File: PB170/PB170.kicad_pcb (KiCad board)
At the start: 4 copper layers, 96.5 x 71.1 mm, 34 parts, among them J1 USB_C_Receptacle_USB2.0-Conne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, J2 USB_B_Micro, Q1 P-MOSFET-MLP_HS, Q2 BC817, SW1 SW_MEC_5E, SW2 SW_MEC_5E, U1 74HC00

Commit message: KiCad crashing fixup, probably
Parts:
- removed J1: USB_C_Receptacle_USB2.0-Connector, PB170:USB_C_Female-16Pin-HPJF
- added RV1: R_POT, PB170:potentiometer10k, F.Cu at (61.6, 90.9)
- added SW3: SW_SPDT, PB170:toggleSwitch, F.Cu at (101.5, 32.3)
- added U2: 74HC08, Housings_SOIC:SOIC-14_3.9x8.7mm_Pitch1.27mm, F.Cu at (127.0, 48.5)
- added U3: 74HC4511D, Housings_SOIC:SOIC-16_3.9x9.9mm_Pitch1.27mm, F.Cu at (127.1, 63.1)
- added U4: HEF4518BT, Housings_SOIC:SOIC-16_3.9x9.9mm_Pitch1.27mm, F.Cu at (116.8, 35.7)
- added U5: 74HC32, Housings_SOIC:SOIC-14_3.9x8.7mm_Pitch1.27mm, F.Cu at (60.6, 35.4)
- J2: footprint Connectors:USB_Micro-B -> PB170:MICRO-USB-SMD_MICROXNJ; moved to F.Cu
- R10: value 220R -> 10k; footprint Resistors_SMD:R_0603 -> Resistor_SMD:R_0603_1608Metric
- moved J2 46.2 mm to (79.1, 92.2)
- moved R11 34.2 mm to (78.7, 83.8)
- moved R10 23.1 mm to (88.6, 36.4)
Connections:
- R10 pad 2: Net-(J1-PadA7) -> GND
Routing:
- net Net-(J2-Pad3): track 3.47 -> 0.00 mm, vias 1 -> 0
- net Net-(J2-Pad2): track 3.11 -> 0.00 mm, vias 1 -> 0

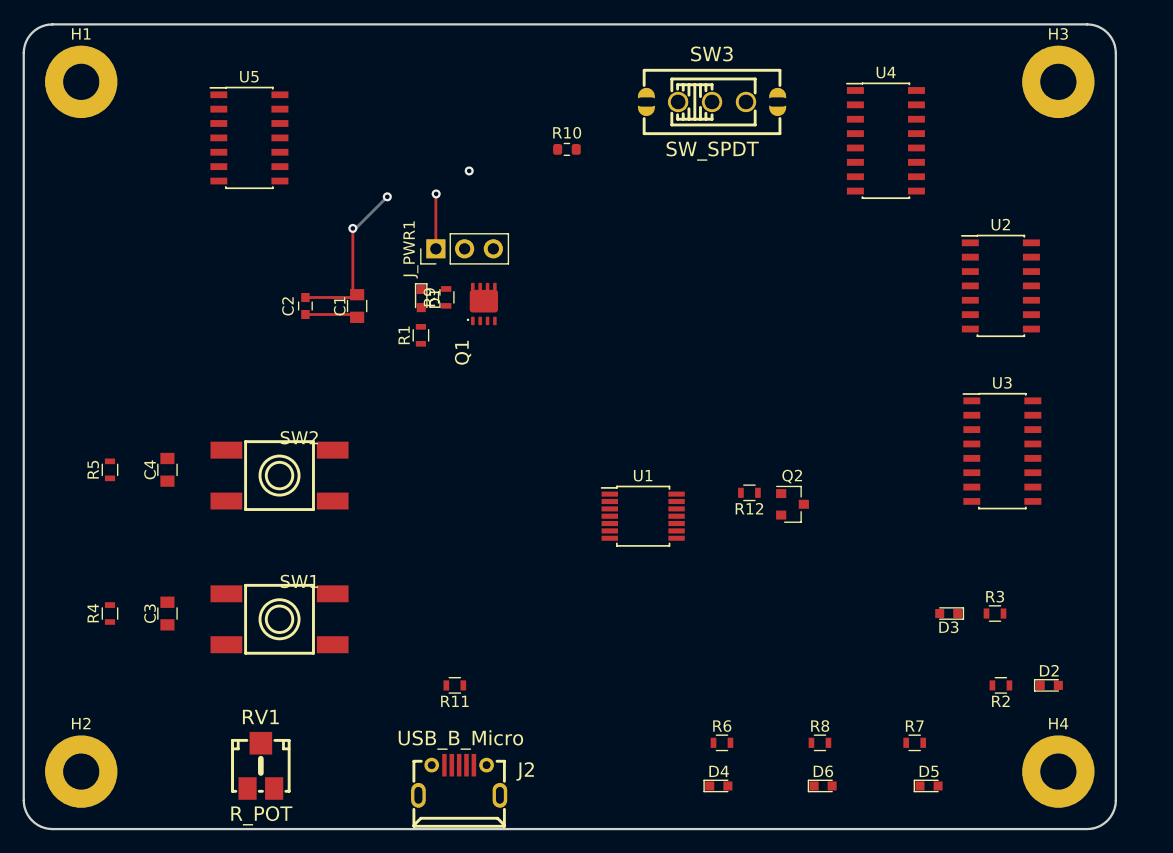
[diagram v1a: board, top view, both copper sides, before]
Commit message: need needs capacitor footprints
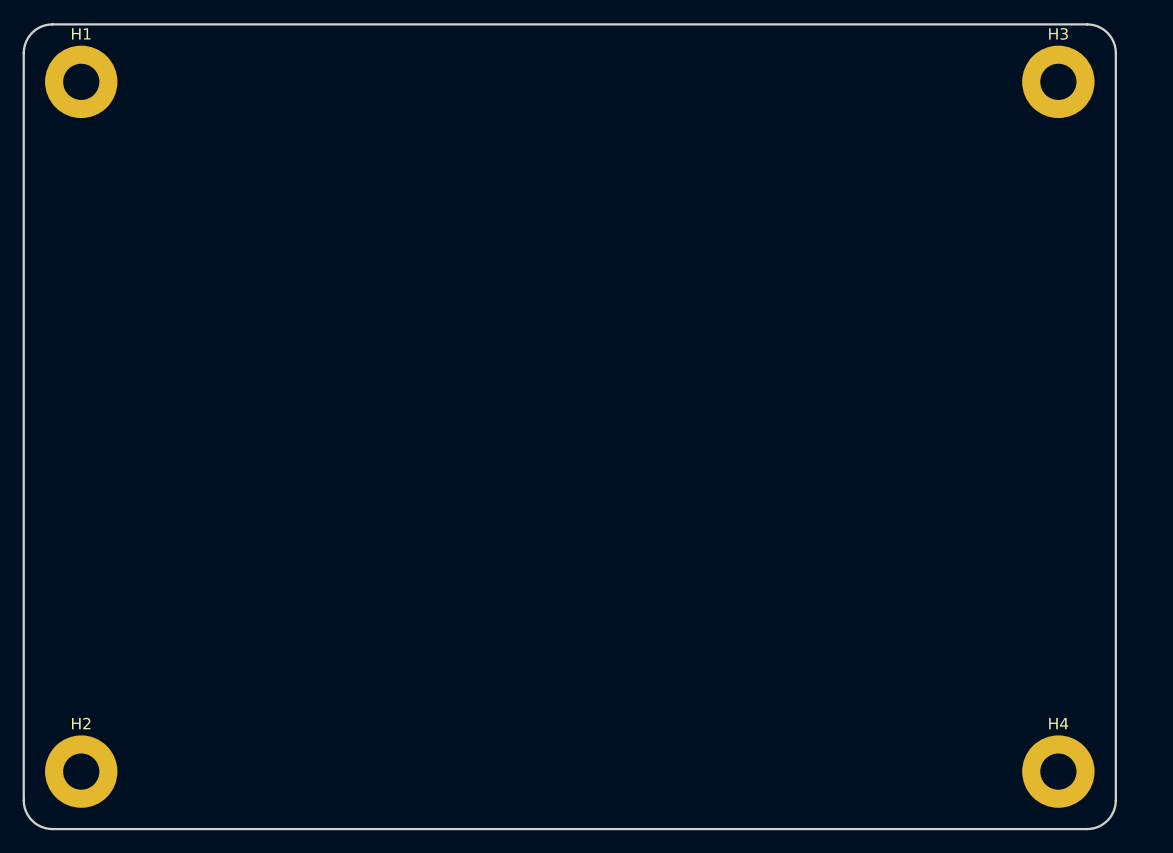
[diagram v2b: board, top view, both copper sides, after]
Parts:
- removed C1, C3, C4: 10uF, Capacitors_SMD:C_0805
- removed C2: 100nF, Capacitors_SMD:C_0603
- removed D1: LED red, LEDs:LED_0603
- removed D2, D3: LED yellow, LEDs:LED_0603
- removed D4: LED green, LEDs:LED_0603
- removed D5: LED blue, LEDs:LED_0603
- removed D6: LED white, LEDs:LED_0603
- removed J2: USB_B_Micro, PB170:MICRO-USB-SMD_MICROXNJ
- removed J_PWR1: Conn_01x03, Pin_Headers:Pin_Header_Straight_1x03_Pitch2.54mm
- removed Q1: P-MOSFET-MLP_HS, PB170:MLP3.3X3.3_HS
- removed Q2: BC817, TO_SOT_Packages_SMD:SOT-23
- removed R1, R11, R12, R7: 220R, Resistors_SMD:R_0603
- removed R10: 10k, Resistor_SMD:R_0603_1608Metric
- removed R2, R3, R6: 180R, Resistors_SMD:R_0603
- removed R4, R5, R9: 10k, Resistors_SMD:R_0603
- removed R8: 130R, Resistors_SMD:R_0603
- removed RV1: R_POT, PB170:potentiometer10k
- removed SW1, SW2: SW_MEC_5E, PB170:TactileSwitch_C381064
- removed SW3: SW_SPDT, PB170:toggleSwitch
- removed U1: 74HC00, Housings_SSOP:TSSOP-14_4.4x5mm_Pitch0.65mm
- removed U2: 74HC08, Housings_SOIC:SOIC-14_3.9x8.7mm_Pitch1.27mm
- removed U3: 74HC4511D, Housings_SOIC:SOIC-16_3.9x9.9mm_Pitch1.27mm
- removed U4: HEF4518BT, Housings_SOIC:SOIC-16_3.9x9.9mm_Pitch1.27mm
- removed U5: 74HC32, Housings_SOIC:SOIC-14_3.9x8.7mm_Pitch1.27mm
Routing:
- net GND: track 32.0 -> 0.00 mm, vias 4 -> 0
- net +5V: track 4.68 -> 0.00 mm

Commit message: 13-02-2021 Martin
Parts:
- added C1: 10uF, PB170:C0805, F.Cu at (126.7, 66.0)
- added C2: 100nF, PB170:C0603, F.Cu at (133.3, 66.0)
- added C3: 10n, PB170:C0402, F.Cu at (121.9, 39.4)
- added C4: 47u, PB170:C0805, F.Cu at (130.5, 39.4)
- added C5: 10uF, PB170:C0805, F.Cu at (58.4, 91.4)
- added C6: 10uF, PB170:C0805, F.Cu at (121.7, 91.4)
- added D1: LED red, PB170:LED0603-R-RD, F.Cu at (125.7, 73.7)
- added D2: LED red, PB170:LED0603-R-RD, F.Cu at (77.1, 82.5)
- added D3: LED red, PB170:LED0603-R-RD, F.Cu at (83.8, 82.5)
- added D4: LED red, PB170:LED0603-R-RD, F.Cu at (91.0, 82.5)
- added D5: LED red, PB170:LED0603-R-RD, F.Cu at (97.4, 82.5)
- added D6: LED red, PB170:LED0603-R-RD, F.Cu at (104.1, 82.5)
- added J2: USB_B_Micro, PB170:MICRO-USB-SMD_MICROXNJ, F.Cu at (133.3, 81.3)
- added R1: 220R, PB170:R0603, F.Cu at (133.3, 73.7)
- added R10: 220R, PB170:R0603, F.Cu at (97.3, 76.2)
- added R11: 220R, PB170:R0603, F.Cu at (125.3, 81.3)
- added R12: 220R, PB170:R0603, F.Cu at (103.7, 76.2)
- added R2: 10k, PB170:R0603, F.Cu at (111.8, 29.2)
- added R3: 10k, PB170:R0603, F.Cu at (118.1, 29.2)
- added R4: 10k, PB170:R0603, F.Cu at (68.1, 91.4)
- added R5: 10k, PB170:R0603, F.Cu at (112.6, 91.4)
- added R6: 220R, PB170:R0603, F.Cu at (77.5, 76.2)
- added R7: 220R, PB170:R0603, F.Cu at (83.8, 76.2)
- added R8: 220R, PB170:R0603, F.Cu at (91.4, 76.2)
- added SW1: SW_MEC_5E, PB170:TactileSwitch_C381064, F.Cu at (78.7, 91.4)
- added SW2: SW_MEC_5E, PB170:TactileSwitch_C381064, F.Cu at (100.7, 91.2)
- added U1: 74HC00, PB170:TSSOP-14_L5.0-W4.4-P0.65-LS6.4-BL, F.Cu at (49.5, 53.3)
- added U10: 74HC74, PB170:TSSOP-14_L5.0-W4.4-P0.65-LS6.4-BL, F.Cu at (60.3, 38.4)
- added U11: 74HC74, PB170:TSSOP-14_L5.0-W4.4-P0.65-LS6.4-BL, F.Cu at (72.4, 38.4)
- added U12: 74HC74, PB170:TSSOP-14_L5.0-W4.4-P0.65-LS6.4-BL, F.Cu at (85.1, 38.4)
- added U13: 74HC74, PB170:TSSOP-14_L5.0-W4.4-P0.65-LS6.4-BL, F.Cu at (97.1, 38.4)
- added U14: NE555DR, PB170:SOIC-8_L4.9-W3.9-P1.27-LS6.0-BL, F.Cu at (114.3, 38.1)
- added U2: 74HC08, PB170:SOIC-14_L8.7-W3.9-P1.27-LS6.0-BL, F.Cu at (63.5, 53.3)
- added U3: 74HC08, PB170:SOIC-14_L8.7-W3.9-P1.27-LS6.0-BL, F.Cu at (78.7, 52.6)
- added U4: 74HC08, PB170:SOIC-14_L8.7-W3.9-P1.27-LS6.0-BL, F.Cu at (94.0, 52.1)
- added U5: 74HC08, PB170:SOIC-14_L8.7-W3.9-P1.27-LS6.0-BL, F.Cu at (109.2, 52.1)
- added U6: 74HC08, PB170:SOIC-14_L8.7-W3.9-P1.27-LS6.0-BL, F.Cu at (125.7, 52.6)
- added U7: 74HC32, PB170:SOIC-14_L8.7-W3.9-P1.27-LS6.0-BL, F.Cu at (73.7, 64.8)
- added U8: 74HC32, PB170:SOIC-14_L8.7-W3.9-P1.27-LS6.0-BL, F.Cu at (90.2, 64.8)
- added U9: 74HC32, PB170:SOIC-14_L8.7-W3.9-P1.27-LS6.0-BL, F.Cu at (108.0, 64.8)

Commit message: FreeRouting is a very useful java application
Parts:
- moved U6 78.3 mm to (53.3, 82.5)
- moved U5 59.0 mm to (53.3, 71.1)
- moved U9 42.4 mm to (66.0, 71.1)
- moved U4 41.6 mm to (53.3, 61.0)
- moved U3 25.5 mm to (53.3, 50.8)
- moved U8 24.4 mm to (66.0, 61.0)
- moved D2 18.2 mm to (80.9, 64.8)
- moved D3 18.2 mm to (87.6, 64.8)
- moved D4 18.2 mm to (94.8, 64.8)
- moved D5 18.2 mm to (101.2, 64.8)
- moved D6 18.2 mm to (108.0, 64.8)
- moved R10 18.2 mm to (101.1, 58.4)
- moved R12 18.2 mm to (107.5, 58.4)
- moved R6 18.2 mm to (81.3, 58.4)
- moved R7 18.2 mm to (87.6, 58.4)
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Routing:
- net +5V: track 0.00 -> 361.7 mm, vias 0 -> 5
- net GND: track 0.00 -> 350.7 mm, vias 0 -> 1
- net SET: track 0.00 -> 126.8 mm, vias 0 -> 3
- net MODE: track 0.00 -> 109.4 mm, vias 0 -> 2
- net !I0: track 0.00 -> 80.0 mm, vias 0 -> 3
- net Q1: track 0.00 -> 78.8 mm, vias 0 -> 4
- net Q0: track 0.00 -> 77.7 mm, vias 0 -> 5
- net Q2: track 0.00 -> 77.4 mm, vias 0 -> 4
- net Q4: track 0.00 -> 77.1 mm, vias 0 -> 4
- net Q3: track 0.00 -> 73.5 mm, vias 0 -> 5
- net !I1: track 0.00 -> 71.6 mm, vias 0 -> 2
- net I1: track 0.00 -> 63.3 mm, vias 0 -> 3
- net I0: track 0.00 -> 60.7 mm, vias 0 -> 2
- net 10: track 0.00 -> 58.0 mm, vias 0 -> 3
- net 11: track 0.00 -> 54.9 mm, vias 0 -> 4
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
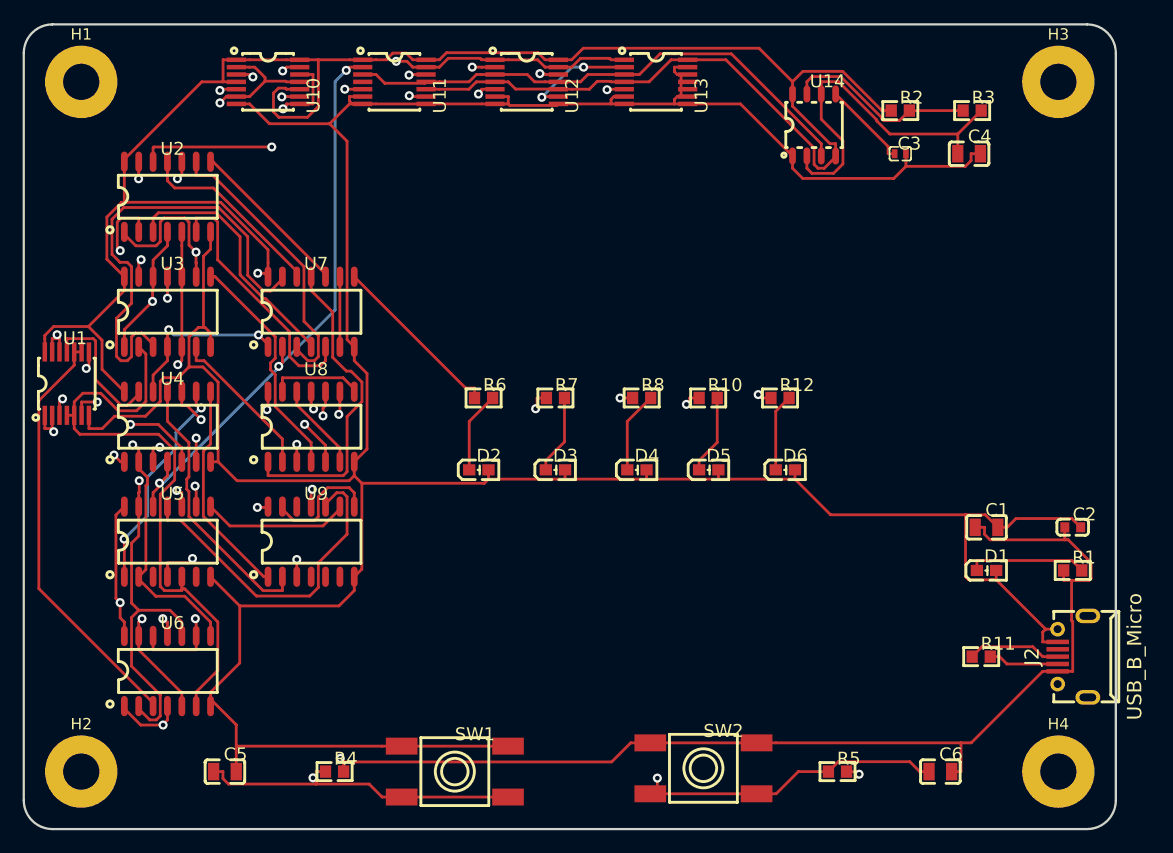
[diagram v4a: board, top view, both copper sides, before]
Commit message: grounded unused pins, added 3D models and photo
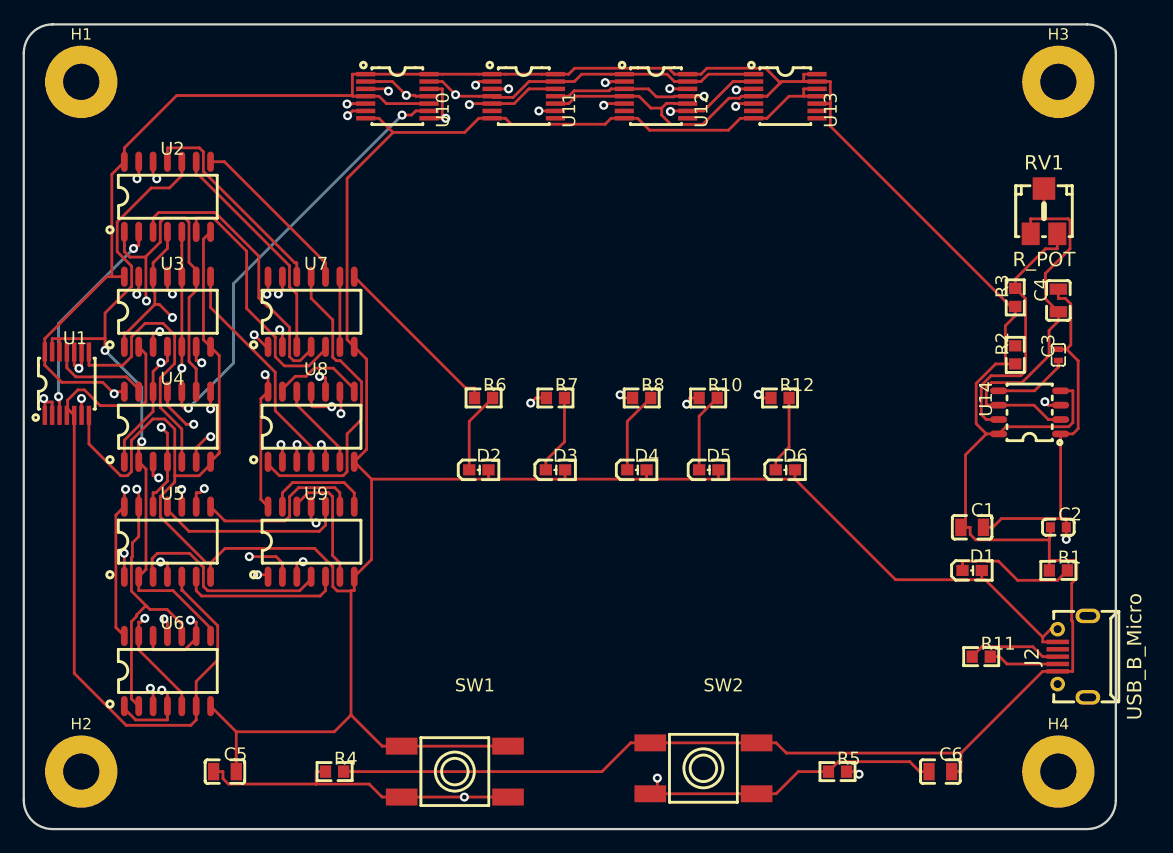
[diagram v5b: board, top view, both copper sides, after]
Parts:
- added RV1: R_POT, PB170:potentiometer10k, F.Cu at (130.8, 41.9)
- moved U14 31.8 mm to (129.5, 59.7), turned to 90 degrees
- moved R2 23.9 mm to (128.3, 54.6), turned to 90 degrees
- moved C3 22.6 mm to (132.1, 54.6), turned to 90 degrees
- moved R3 16.9 mm to (128.3, 49.5), turned to 90 degrees
- moved C4 15.2 mm to (132.1, 49.8), turned to 90 degrees
- moved U13 11.5 mm to (108.0, 31.8)
- moved U10 11.5 mm to (73.7, 31.8)
- moved U11 11.5 mm to (84.8, 31.8)
- moved U12 11.5 mm to (96.5, 31.8)
- moved C1 1.27 mm to (124.5, 69.8)
- moved D1 1.27 mm to (124.5, 73.7)
- moved C2 1.27 mm to (132.1, 69.8)
- moved R1 1.27 mm to (132.1, 73.7)
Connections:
- R3 pad 1: Net-(R2-Pad2) -> +5V
- R3 pad 2: Net-(C4-Pad1) -> Net-(R3-Pad2)
- U11 pad 4: Net-(U11-Pad4) -> SET
- U11 pad 6: GND -> Net-(U11-Pad6)
- U11 pad 8: GND -> Net-(U11-Pad8)
- U12 pad 6: GND -> Net-(U12-Pad6)
- U12 pad 8: GND -> Net-(U12-Pad8)
- U13 pad 10: GND -> +5V
- U13 pad 13: GND -> +5V
- U13 pad 6: GND -> Net-(U13-Pad6)
- U13 pad 8: GND -> Net-(U13-Pad8)
- U13 pad 9: GND -> Net-(U13-Pad9)
- U14 pad 7: Net-(R2-Pad2) -> Net-(R3-Pad2)
- U9 pad 4: Net-(U9-Pad4) -> Net-(U5-Pad3)
- U9 pad 5: Net-(U9-Pad5) -> Net-(U5-Pad6)
- U9 pad 6: Net-(U9-Pad6) -> Net-(U9-Pad12)
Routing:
- net CLOCK: track 46.8 -> 77.7 mm, vias 0 -> 4
- net Net-(U3-Pad3): track 41.0 -> 15.5 mm, vias 0 -> 2
- net Net-(R3-Pad2): track 0.00 -> 23.4 mm
- net Q0: track 77.7 -> 99.3 mm, vias 5 -> 3
- net Net-(U5-Pad3): track 0.00 -> 18.9 mm
- net Net-(R2-Pad2): track 17.1 -> 0.00 mm
- net Net-(U5-Pad6): track 0.00 -> 14.3 mm
- net Net-(U5-Pad11): track 29.4 -> 16.9 mm
- net 01: track 53.9 -> 65.8 mm
- net Net-(U9-Pad12): track 0.00 -> 11.3 mm
- net Q2: track 77.4 -> 88.2 mm
- net Net-(U1-Pad8): track 14.7 -> 24.3 mm, vias 2 -> 0
- net +5V: track 361.7 -> 353.5 mm, vias 5 -> 4
- net Q1: track 78.8 -> 86.7 mm
- net GND: track 350.7 -> 343.9 mm, vias 1 -> 2
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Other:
- board text added: "MODE"
- board text added: "SET"
